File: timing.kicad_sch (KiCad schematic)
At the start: 4 parts, among them Y2 XRCGB32M000F2P01R0

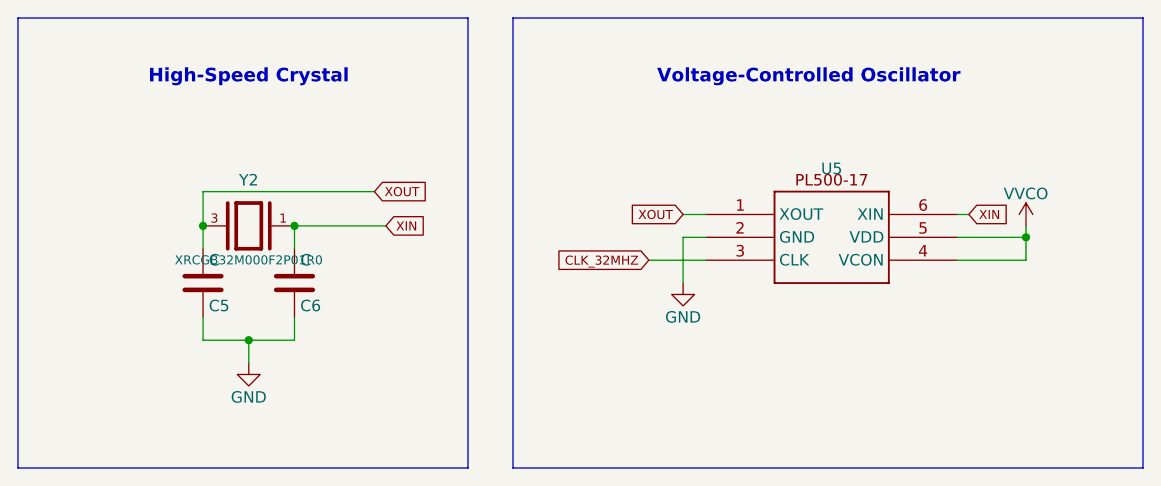
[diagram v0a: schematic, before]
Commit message: isolated v sources
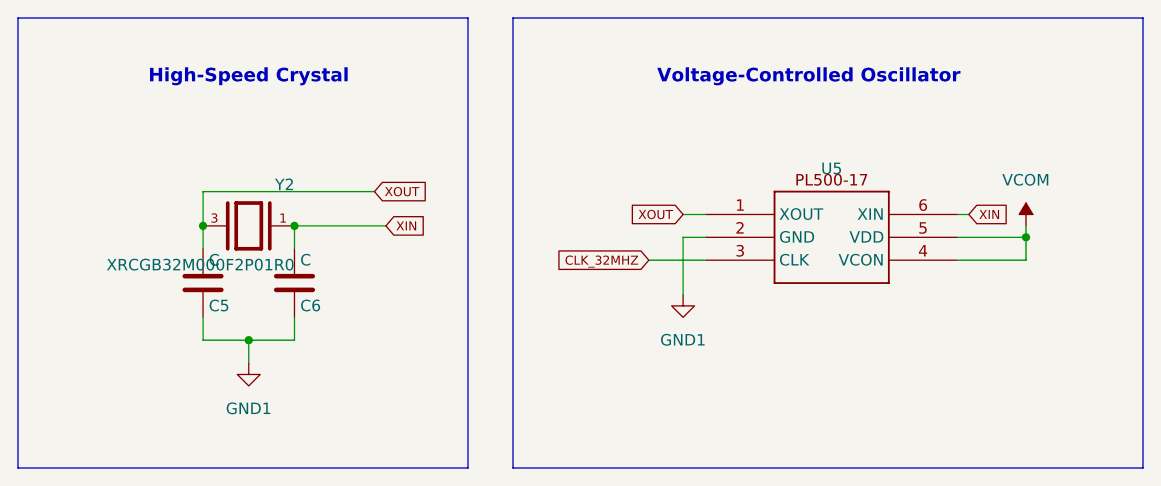
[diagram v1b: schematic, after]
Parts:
- Y2: symbol XRCGB32M000F2P01R0:XRCGB32M000F2P01R0 -> CRYSTAL_32MHz:XRCGB32M000F2P01R0
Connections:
- net GND renamed GND1
- net VVCO renamed VCOM
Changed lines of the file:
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@@
 	(wire
 		(pts
-			(xy 88.9 39.37) (xy 88.9 44.45)
+			(xy 88.9 39.37) (xy 88.9 45.72)
 		)
 		(stroke
@@
 	(wire
 		(pts
-			(xy 127 39.37) (xy 127 38.1)
+			(xy 127 38.1) (xy 127 39.37)
 		)
 		(stroke
@@
 	)
 	(symbol
-		(lib_id "power:GND")
-		(at 88.9 44.45 0)
-		(mirror y)
+		(lib_id "power:GND1")
+		(at 88.9 45.72 0)
 		(unit 1)
 		(exclude_from_sim no)
@@
 		(on_board yes)
 		(dnp no)
-		(property "Reference" "#PWR025"
+		(fields_autoplaced yes)
+		(property "Reference" "#PWR012"
+			(at 88.9 52.07 0)
+			(effects
+				(font
+					(size 1.27 1.27)
+				)
+				(hide yes)
+			)
+		)
+		(property "Value" "GND1"
 			(at 88.9 50.8 0)
 			(effects
@@
 					(size 1.27 1.27)
 				)
-				(hide yes)
-			)
-		)
-		(property "Value" "GND"
-			(at 88.9 48.26 0)
-			(effects
-				(font
-					(size 1.27 1.27)
-				)
 			)
 		)
 		(property "Footprint" ""
-			(at 88.9 44.45 0)
+			(at 88.9 45.72 0)
 			(effects
 				(font
@@
 		)
 		(property "Datasheet" ""
-			(at 88.9 44.45 0)
-			(effects
-				(font
-					(size 1.27 1.27)
-				)
-				(hide yes)
-			)
-		)
-		(property "Description" "Power symbol creates a global label with name \"GND\" , ground"
-			(at 88.9 44.45 0)
+			(at 88.9 45.72 0)
+			(effects
+				(font
+					(size 1.27 1.27)
+				)
+				(hide yes)
+			)
+		)
+		(property "Description" "Power symbol creates a global label with name \"GND1\" , ground"
+			(at 88.9 45.72 0)
 			(effects
 				(font
@@
 			(project "apex"
 				(path "/84b8b555-aaa5-476b-b0f2-2d0f894bf0e6/ab1b63b7-7528-435b-84e9-ba5a60716e92"
-					(reference "#PWR025")
+					(reference "#PWR012")
 					(unit 1)
 				)
@@
 	)
 	(symbol
-		(lib_id "XRCGB32M000F2P01R0:XRCGB32M000F2P01R0")
+		(lib_id "CRYSTAL_32MHz:XRCGB32M000F2P01R0")
 		(at 40.64 38.1 0)
 		(mirror y)
@@
 		(dnp no)
 		(property "Reference" "Y2"
-			(at 40.64 33.02 0)
-			(effects
-				(font
-					(size 1.27 1.27)
-				)
+			(at 45.7278 34.2841 0)
+			(effects
+				(font
+					(size 1.27 1.27)
+				)
+				(justify left bottom)
 			)
 		)
 		(property "Value" "XRCGB32M000F2P01R0"
-			(at 40.64 41.91 0)
-			(effects
-				(font
-					(size 1 1)
-				)
+			(at 45.7344 43.1944 0)
+			(effects
+				(font
+					(size 1.27 1.27)
+				)
+				(justify left bottom)
 			)
 		)
@@
 	)
 	(symbol
-		(lib_id "power:GND")
+		(lib_id "power:GND1")
 		(at 40.64 53.34 0)
-		(mirror y)
 		(unit 1)
 		(exclude_from_sim no)
@@
 		(on_board yes)
 		(dnp no)
-		(property "Reference" "#PWR012"
+		(fields_autoplaced yes)
+		(property "Reference" "#PWR051"
 			(at 40.64 59.69 0)
 			(effects
@@
 			)
 		)
-		(property "Value" "GND"
-			(at 40.64 57.15 0)
+		(property "Value" "GND1"
+			(at 40.64 58.42 0)
 			(effects
 				(font
@@
 			)
 		)
-		(property "Description" "Power symbol creates a global label with name \"GND\" , ground"
+		(property "Description" "Power symbol creates a global label with name \"GND1\" , ground"
 			(at 40.64 53.34 0)
 			(effects
@@
 		)
 		(instances
-			(project "apex"
+			(project ""
 				(path "/84b8b555-aaa5-476b-b0f2-2d0f894bf0e6/ab1b63b7-7528-435b-84e9-ba5a60716e92"
-					(reference "#PWR012")
+					(reference "#PWR051")
 					(unit 1)
 				)
@@
 	)
 	(symbol
-		(lib_id "power:VDD")
+		(lib_id "power:VCOM")
 		(at 127 38.1 0)
 		(unit 1)
@@
 		(on_board yes)
 		(dnp no)
-		(property "Reference" "#PWR026"
+		(fields_autoplaced yes)
+		(property "Reference" "#PWR032"
 			(at 127 41.91 0)
 			(effects
@@
 			)
 		)
-		(property "Value" "VVCO"
-			(at 127 34.544 0)
+		(property "Value" "VCOM"
+			(at 127 33.02 0)
 			(effects
 				(font
@@
 			)
 		)
-		(property "Description" "Power symbol creates a global label with name \"VDD\""
+		(property "Description" "Power symbol creates a global label with name \"VCOM\""
 			(at 127 38.1 0)
 			(effects
@@
 			(project "apex"
 				(path "/84b8b555-aaa5-476b-b0f2-2d0f894bf0e6/ab1b63b7-7528-435b-84e9-ba5a60716e92"
-					(reference "#PWR026")
+					(reference "#PWR032")
 					(unit 1)
 				)

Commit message: added sheets
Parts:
- U5: footprint (none) -> Package_SO:SOIC-8-1EP_3.9x4.9mm_P1.27mm_EP2.41x3.3mm
- Y2: footprint XRCGB32M000F2P01R0:OSC_XRCGB32M000F2P01R0 -> CRYSTAL_32MHZ:OSC_XRCGB32M000F2P01R0
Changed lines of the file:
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@@
 			)
 		)
-		(property "Footprint" "XRCGB32M000F2P01R0:OSC_XRCGB32M000F2P01R0"
+		(property "Footprint" "CRYSTAL_32MHZ:OSC_XRCGB32M000F2P01R0"
 			(at 40.64 38.1 0)
 			(effects
@@
 			)
 		)
-		(property "Footprint" ""
+		(property "Footprint" "Package_SO:SOIC-8-1EP_3.9x4.9mm_P1.27mm_EP2.41x3.3mm"
 			(at 105.41 34.29 0)
 			(effects
